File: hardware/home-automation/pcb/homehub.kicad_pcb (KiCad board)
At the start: 2 copper layers, 137.8 x 96.6 mm, 67 parts, among them J1 2P 5.08mm, J2 5P 5.08mm, K1 SRD-05VDC-SL-C, K2 SRD-05VDC-SL-C, K3 SRD-05VDC-SL-C, K4 SRD-05VDC-SL-C, Q1 S8050, Q2 S8050, Q3 S8050, Q4 S8050, SW1 Tactile 6mm, SW2 Tactile 6mm, SW3 Tactile 6mm, SW4 Tactile 6mm, SW5 Tactile 6mm, U1 ESP32-WROOM-32E (4MB), U2 AMS1117-3.3, U3 PC817, U4 PC817, U5 PC817, U6 PC817

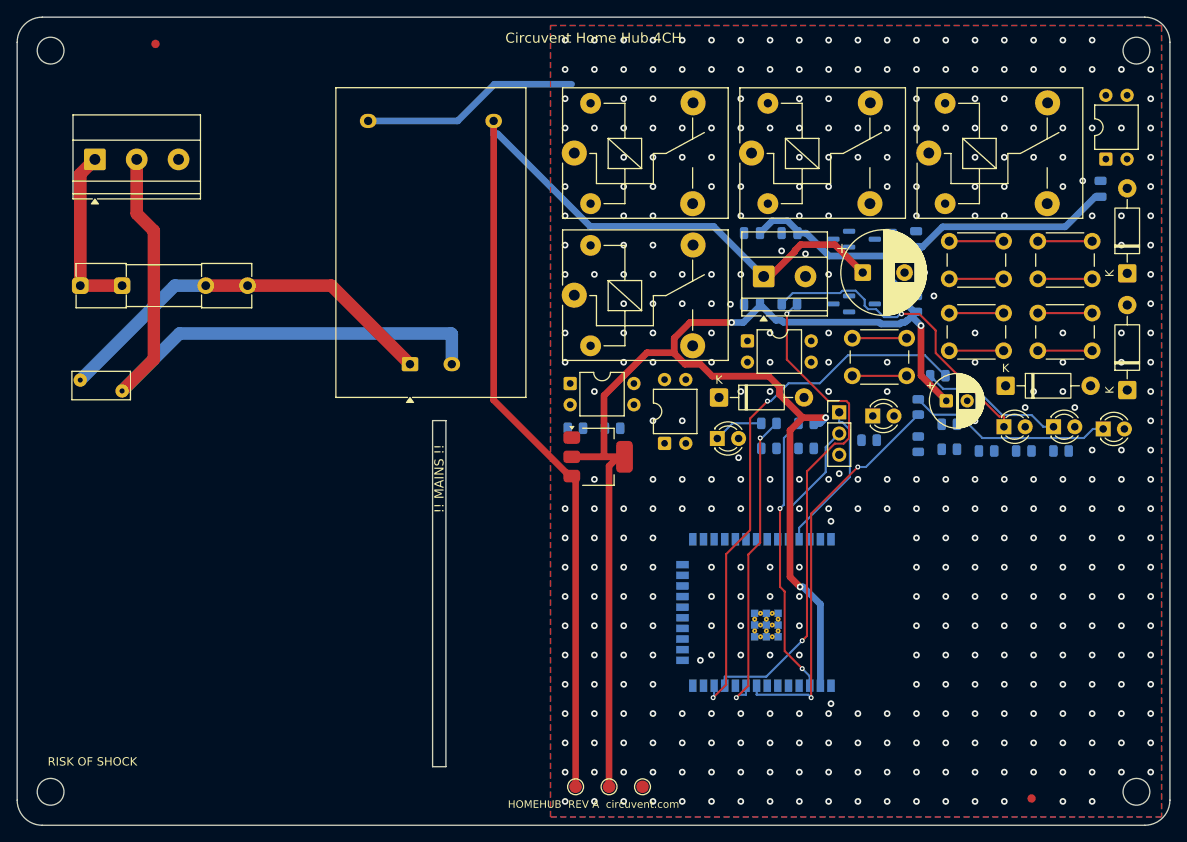
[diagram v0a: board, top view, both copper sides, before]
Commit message: hardware: fix mains isolation barrier gaps, add load-controller PCB
Adds the 13th board (ultra-compact dual-channel load controller: ESP32-C3,
opto+relay channel, MOSFET PWM channel, USB-C, AP2112K LDO, USBLC6 ESD) and
regenerates all 12 existing boards, which were stale with respect to earlier
relay-pinout and LED-polarity fixes.

The substantive change is to the mains isolation barrier. It is a keepout band
the router must not cross, deliberately cut where a component straddles it
because there the isolation is provided by the part's package. Three linked
defects made those cuts unsafe, each only visible once the previous was fixed:

1. The cut removed the barrier across the full band width for the straddling
   part's whole height, while the ISO_BRIDGE area that excuses the gap covered
   only the part itself. The router used the leftover strip beside the part to
   bring +5V within 6.99 mm of AC_N against an 8.0 mm reinforced creepage rule.
2. Straddling parts can overlap in y, so cutting per part put one part's
   keepout on another part's pads. The exempt x-ranges are now unioned per
   strip by a sweep line.
3. The rule only relaxes for items insideArea('ISO_BRIDGE'). With the hole the
   same size as the area, a track could hug the hole's edge without being
   contained in it, so the rule fired anyway and the router had no way to know.
   The hole is now the part's pad bbox + 0.3 mm, strictly inside ISO_BRIDGE at
   the footprint bbox + 0.6 mm.

The tighter hole leaves mains nets less room to reach bridge pads, so some
boards report more unconnected items. That is deliberate: those are documented
hand-routing items, whereas a creepage violation is a safety defect.

Also fixed in the generator:
- _pad_shape() derived a pad's layers from PAD::GetLayer(), which returns F.Cu
  even for pads on B.Cu. Every back-side pad became a phantom obstacle on the
  front, blocking legal paths there while hiding the real one behind. Only
  IsOnLayer() is truthful.
- Castella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
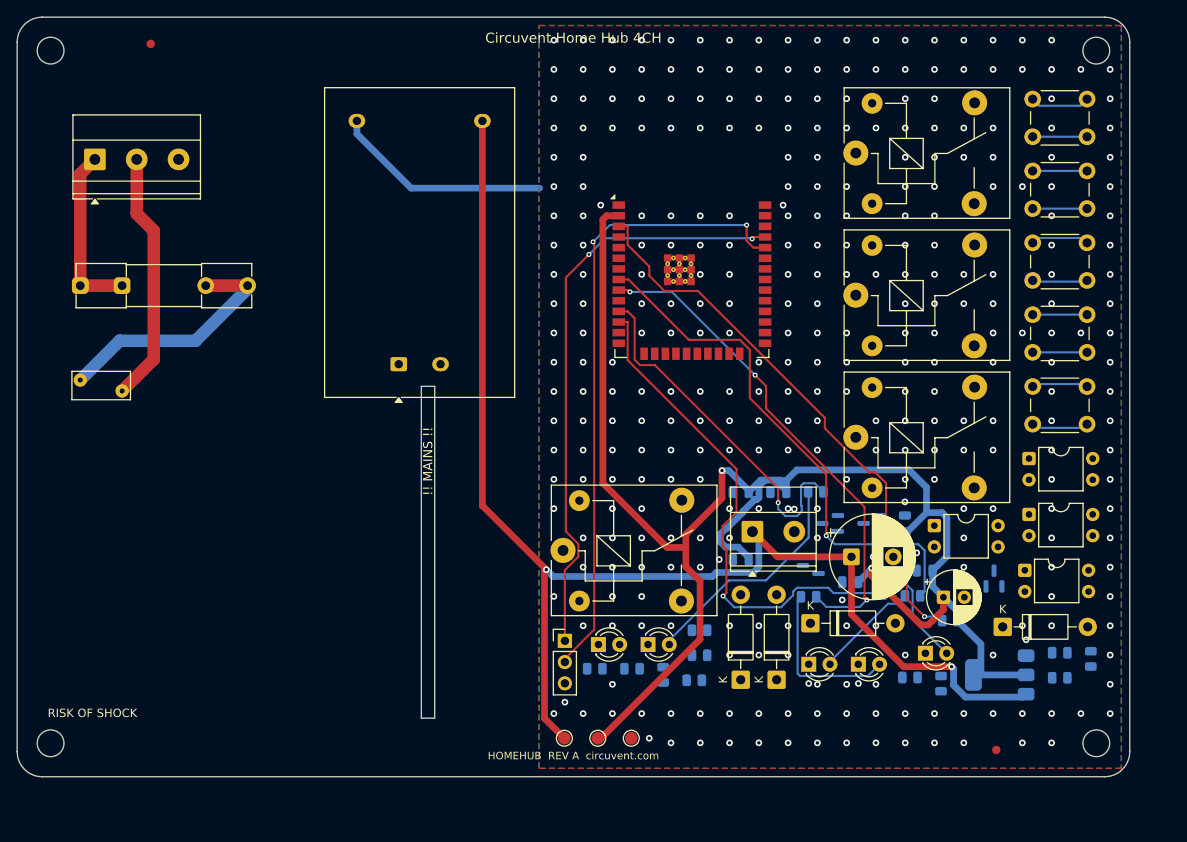
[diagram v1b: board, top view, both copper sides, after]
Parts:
- U1: moved to F.Cu
- U2: moved to B.Cu
- moved D1 67.0 mm to (186.5, 159.2)
- moved R7 63.8 mm to (224.6, 156.0)
- moved R8 63.5 mm to (228.3, 156.7), turned to 90 degrees
- moved C3 56.2 mm to (186.5, 136.8), turned to 180 degrees
- moved U2 54.6 mm to (217.5, 158.6), turned to 180 degrees
- moved D2 54.4 mm to (190.8, 159.2)
- moved R16 51.7 mm to (180.9, 159.3)
- moved LED1 49.9 mm to (175.4, 155.0)
- moved U5 46.7 mm to (209.6, 140.8)
- moved U6 45.7 mm to (220.5, 146.1), turned to 0 degrees
- moved LED3 45.1 mm to (194.6, 157.4)
- moved U1 44.9 mm to (180.7, 107.7), turned to 0 degrees
- moved C6 43.7 mm to (186.5, 144.8), turned to 180 degrees
- moved D4 43.6 mm to (217.8, 152.9)
- moved JP 42.7 mm to (165.5, 154.6)
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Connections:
- LED1 pad 1: 0_A -> GND
- LED1 pad 2: GND -> 0_A
- LED2 pad 1: 1_A -> GND
- LED2 pad 2: GND -> 1_A
- LED3 pad 1: 2_A -> GND
- LED3 pad 2: GND -> 2_A
- LED4 pad 1: 3_A -> GND
- LED4 pad 2: GND -> 3_A
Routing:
- net UART_RX: track 15.2 -> 75.4 mm, vias 0 -> 2
- net UART_TX: track 18.4 -> 70.6 mm, vias 0 -> 2
- net AC_N: track 76.0 -> 30.1 mm
- net +3V3: track 222.0 -> 185.3 mm, vias 4 -> 2
- net EN: track 33.7 -> 67.5 mm, vias 2 -> 1
- net 3: track 37.3 -> 59.8 mm, vias 2 -> 3
- net AC_L_FUSED: track 48.0 -> 29.9 mm
- net 0: track 60.2 -> 42.9 mm, vias 2 -> 1
- net 2: track 47.4 -> 63.3 mm, vias 2 -> 1
- net +5V: track 139.6 -> 155.0 mm, vias 0 -> 2
- net 3_A: track 6.00 -> 19.8 mm
- net 2_A: track 24.6 -> 12.5 mm
- net 0_A: track 37.0 -> 27.8 mm, vias 1 -> 0
- net 1_A: track 17.3 -> 13.4 mm
- net 1: track 64.2 -> 61.4 mm, vias 2 -> 1
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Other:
- board size 137.8 x 96.6 mm -> 133 x 90.8 mm

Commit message: Release 1.10.0, and stop shipping permissions the app never uses
Cut 1.10.0 (versionCode 12) and built it: AAB 38 MB, APK 83 MB, signed with the
upload key, JS bundle embedded.

Checking the generated manifest before writing the Play listing turned up
permissions no one had asked for. Every one of them is printed on the store page
for users to read before they install:

  RECORD_AUDIO          expo-camera asks for the microphone so video can be
                        recorded with sound. This app only ever puts the camera
                        in barcode mode to read a QR label, and expo-speech is
                        output-only - it speaks, it does not listen. Left in,
                        Play lists "Microphone" against a home-control app,
                        which is alarming, unexplainable and untrue.
  SYSTEM_ALERT_WINDOW   React Native's development overlay, useless in a release
                        build and shown to users as "Display over other apps".
  READ/WRITE_EXTERNAL_STORAGE
                        Legacy storage access nothing here touches.

Stripped via android.blockedPermissions. That emits tools:node="remove", which
is a merge instruction rather than a guarantee, so it was checked against the
finished artifact with aapt2 rather than the source manifest - all four are
absent from the APK.

NEARBY_WIFI_DEVICES now carries neverForLocation. Android otherwise treats it as
location-capable, because knowing which networks are in range is enough to place
someone, and Play's data safety review treats it the same way. The app uses it
only to join a new device's setup hotspot. That flag is a promise, so the plugin
says plainly that it has to come off if scan results are ever used positionally.

What is left is defensible: location for Wi-Fi onboarding (Android requires it),
camera for the QR label, nearby-devices flagged as non-positional.

Added mobile/store/listing with the text Play asks for - title, short and full
descriptions, and what'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
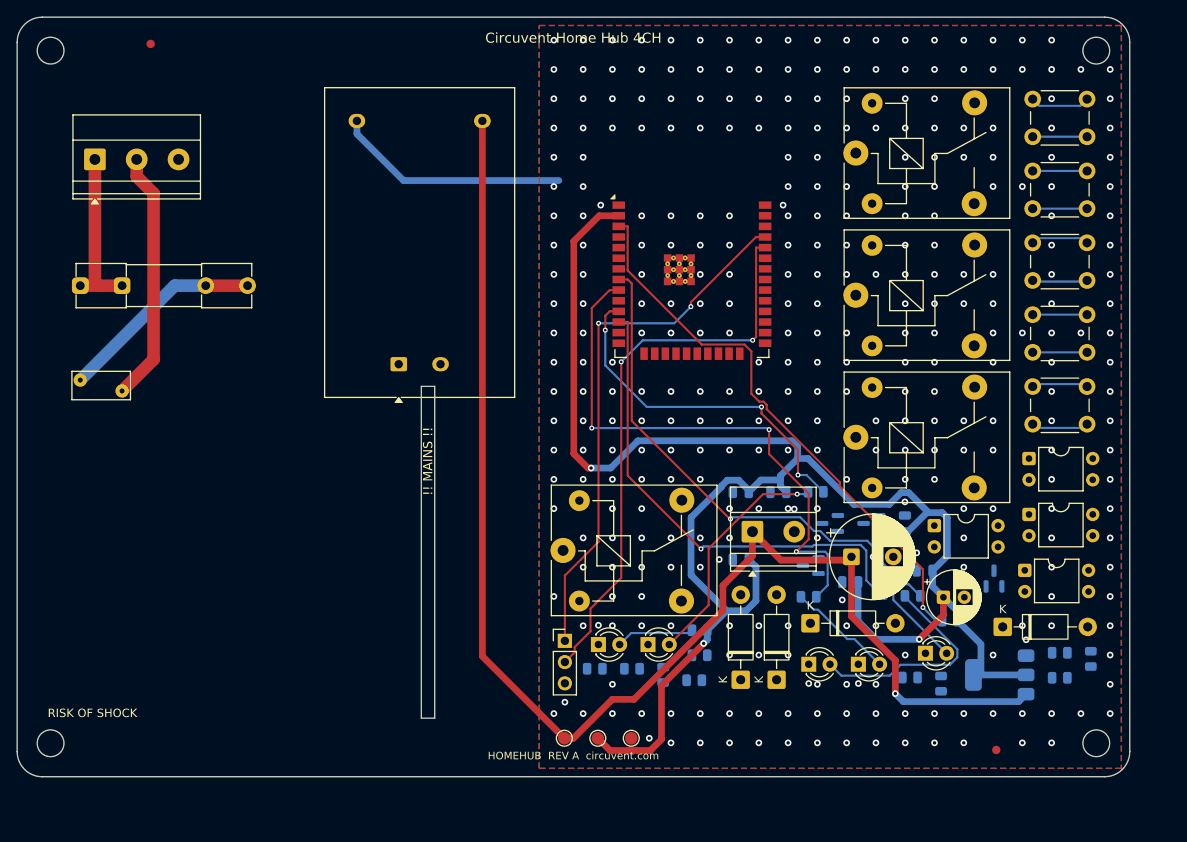
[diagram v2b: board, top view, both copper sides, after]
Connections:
- LED0 pad 1: N$LED0.1 -> GND
- LED0 pad 2: N$LED0.2 -> LED0_A
- R6 pad 1: N$R6.1 -> +3V3
- R6 pad 2: N$R6.2 -> LED0_A
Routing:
- net +3V3: track 185.3 -> 204.1 mm, vias 2 -> 3
- net 2_A: track 12.5 -> 26.6 mm
- net LED0_A: track 0.00 -> 9.35 mm
- net UART_RX: track 75.4 -> 67.8 mm
- net +5V: track 155.0 -> 162.3 mm, vias 2 -> 1
- net 3_A: track 19.8 -> 12.7 mm
- net 3: track 59.8 -> 66.4 mm
- net UART_TX: track 70.6 -> 64.1 mm
- net AC_L_FUSED: track 29.9 -> 24.7 mm
- net 1: track 61.4 -> 58.2 mm
- net GND: track 26.1 -> 28.0 mm, vias 339 -> 340
- net 1_A: track 13.4 -> 11.9 mm
- net 2: track 63.3 -> 62.0 mm
- net 0: track 42.9 -> 42.3 mm, vias 1 -> 3
- net AC_L: track 20.8 -> 20.3 mm
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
